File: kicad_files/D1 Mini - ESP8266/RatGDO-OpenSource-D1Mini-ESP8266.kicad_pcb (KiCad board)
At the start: 2 copper layers, 51.8 x 65.8 mm, 23 parts, among them J1 Screw_Terminal_01x03, J2 Conn_01x10, J3 Screw_Terminal_01x02, Q1 2N7002, Q2 AO3400A, Q3 AO3400A, Q4 AO3400A, U1 WeMos_D1_mini

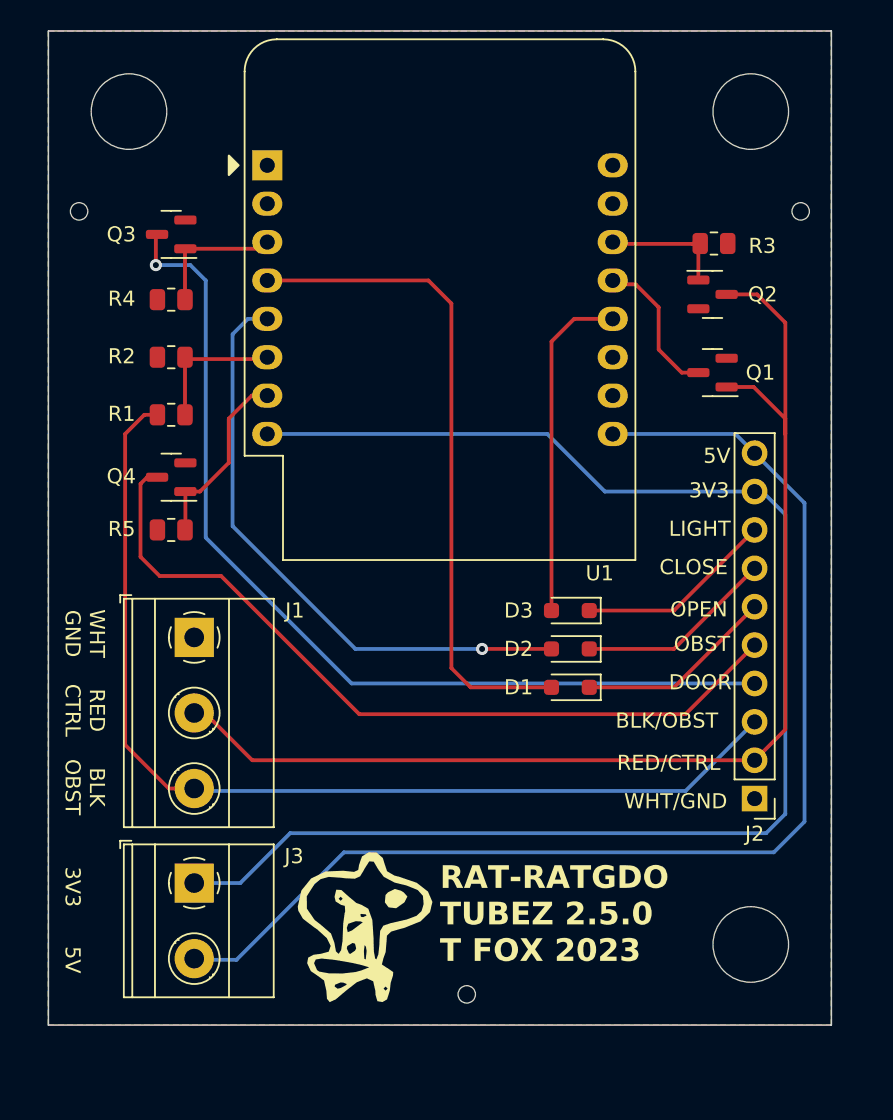
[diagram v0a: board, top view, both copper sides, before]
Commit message: Addition of 12V DC DC supply
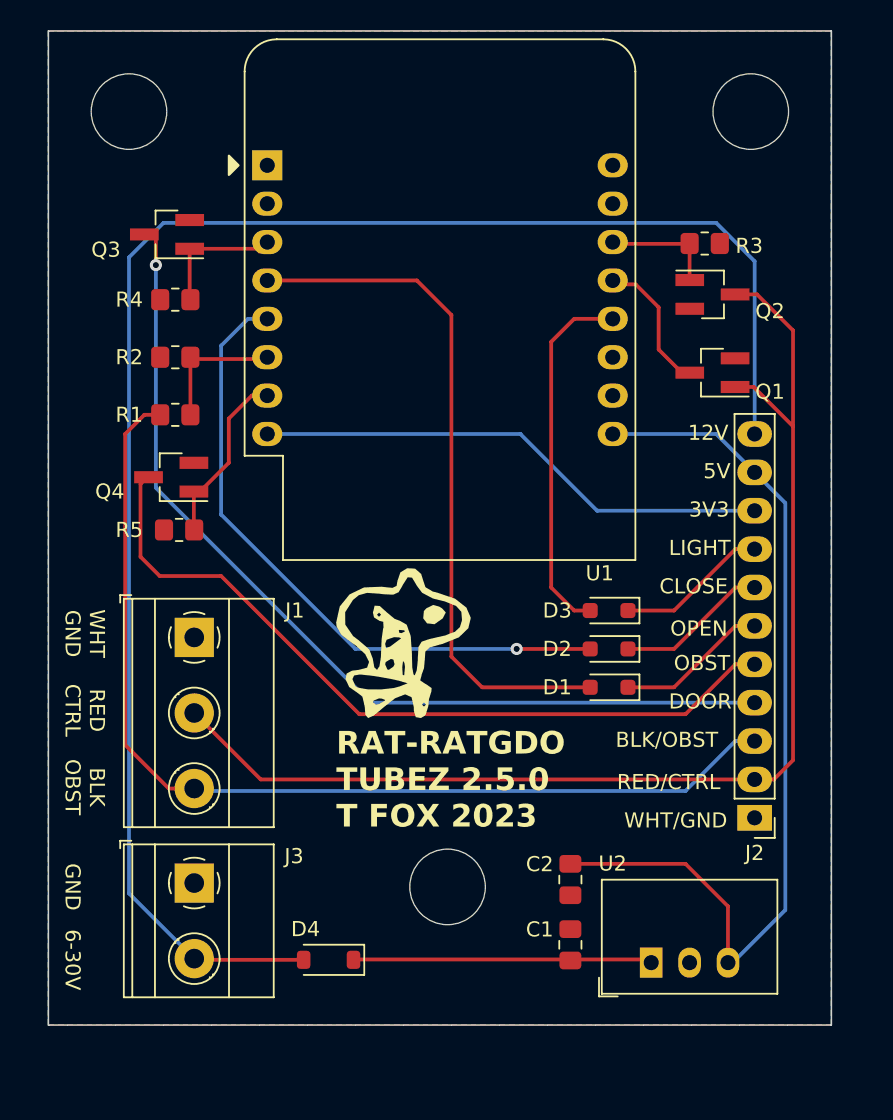
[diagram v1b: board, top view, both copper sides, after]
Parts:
- removed the REF** at (164.8, 69.1)
- removed the REF** at (117.1, 69.1)
- removed the REF** at (142.7, 120.9)
- added C1: 10uF/50V, Capacitor_SMD:C_0805_2012Metric_Pad1.18x1.45mm_HandSolder, F.Cu at (149.6, 117.6)
- added C2: 22uF/10V, Capacitor_SMD:C_0805_2012Metric_Pad1.18x1.45mm_HandSolder, F.Cu at (149.6, 113.3)
- added D4: B5819W, Diode_SMD:D_SOD-123, F.Cu at (133.6, 118.6)
- added U2: K7805-500R3, Converter_DCDC:Converter_DCDC_RECOM_R-78HB-0.5_THT, F.Cu at (160.0, 118.8)
- J2: value Conn_01x10 -> Conn_01x11; footprint Connector_PinHeader_2.54mm:PinHeader_1x10_P2.54mm_Vertical -> Connector_PinHeader_2.54mm:PinHeader_1x11_P2.54mm_Vertical
- Q1, Q2, Q3, Q4: footprint Package_TO_SOT_SMD:SOT-23 -> Package_TO_SOT_SMD:SOT-23_Handsoldering
- R1, R2, R3, R4, R5: footprint Resistor_SMD:R_0805_2012Metric -> Resistor_SMD:R_0805_2012Metric_Pad1.20x1.40mm_HandSolder
- moved REF** 20.4 mm to (141.5, 113.8)
- moved G*** 19.0 mm to (138.4, 97.5)
- moved D1 2.56 mm to (152.2, 100.6)
- moved D2 2.56 mm to (152.2, 98.0)
- moved D3 2.56 mm to (152.2, 95.5)
- moved J2 1.27 mm to (161.8, 109.2)
- moved R3 0.61 mm to (158.5, 71.2)
- moved R5 0.52 mm to (123.7, 90.2)
- moved Q3 0.28 mm to (122.9, 70.6)
- moved R1 0.27 mm to (123.5, 82.6)
- moved R2 0.27 mm to (123.5, 78.7)
- moved R4 0.27 mm to (123.5, 74.9)
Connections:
- J3 pad 1: +3V3 -> GND
- J3 pad 2: +5V -> +12V
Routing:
- net +12V: track 0.00 -> 109.9 mm
- net +3V3: track 96.1 -> 34.4 mm
- net Net-(D4-K): track 0.00 -> 19.7 mm
- net +5V: track 79.2 -> 60.7 mm
- net Net-(D2-A): track 39.9 -> 43.1 mm
- net DC_CLOSE: track 13.2 -> 10.1 mm
- net DC_OPEN: track 13.2 -> 10.1 mm
- net DC_LIGHT: track 13.2 -> 10.1 mm
- net RED/CTRL: track 79.0 -> 81.3 mm
- net Net-(D3-A): track 22.5 -> 24.2 mm
- net Net-(D1-A): track 44.1 -> 45.8 mm
- net /ESP_RX: track 9.84 -> 8.59 mm
- net STS_OBST: track 53.0 -> 51.8 mm
- net Net-(Q4-G): track 12.3 -> 11.3 mm
- net STS_DOOR: track 62.8 -> 62.0 mm
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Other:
- board text added: "12V"
- board text added: "6-30V"

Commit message: rename
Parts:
- removed C1: 10uF/50V, Capacitor_SMD:C_0805_2012Metric_Pad1.18x1.45mm_HandSolder
- removed C2: 22uF/10V, Capacitor_SMD:C_0805_2012Metric_Pad1.18x1.45mm_HandSolder
- removed D1, D2, D3: 1N4148WS, Diode_SMD:D_SOD-323_HandSoldering
- removed D4: B5819W, Diode_SMD:D_SOD-123
- removed G***: LOGO, LOGO
- removed Q3, Q4: AO3400A, Package_TO_SOT_SMD:SOT-23_Handsoldering
- removed R4, R5: 10k, Resistor_SMD:R_0805_2012Metric_Pad1.20x1.40mm_HandSolder
- removed U2: K7805-500R3, Converter_DCDC:Converter_DCDC_RECOM_R-78HB-0.5_THT
- added REF**: MountingHole_5mm, MountingHole:MountingHole_5mm, F.Cu at (120.7, 118.1)
- J2: value Conn_01x11 -> Screw_Terminal_01x03; footprint Connector_PinHeader_2.54mm:PinHeader_1x11_P2.54mm_Vertical -> Connector_Phoenix_MC:PhoenixContact_MCV_1,5_3-G-3.5_1x03_P3.50mm_Vertical
- J3: value Screw_Terminal_01x02 -> Screw_Terminal_01x03; footprint TerminalBlock_Phoenix:TerminalBlock_Phoenix_MKDS-1,5-2_1x02_P5.00mm_Horizontal -> Connector_PinSocket_2.54mm:PinSocket_1x03_P2.54mm_Vertical
- Q1, Q2: footprint Package_TO_SOT_SMD:SOT-23_Handsoldering -> Package_TO_SOT_SMD:SOT-23
- R1, R2, R3: footprint Resistor_SMD:R_0805_2012Metric_Pad1.20x1.40mm_HandSolder -> Resistor_SMD:R_0805_2012Metric
- moved J3 22.7 mm to (147.3, 111.8), turned to 90 degrees
- moved J1 21.7 mm to (129.7, 118.4), turned to 0 degrees
- moved REF** 21.5 mm to (162.6, 118.1)
- moved J2 18.2 mm to (146.7, 119.4), turned to 0 degrees
- moved REF** 1.44 mm to (162.6, 63.5)
- moved REF** 1.05 mm to (120.7, 63.5)
- moved R1 0.27 mm to (123.2, 82.5)
- moved R2 0.27 mm to (123.2, 78.7)
- moved Q1 0.15 mm to (159.2, 79.8)
- moved R3 0.14 mm to (158.6, 71.2), turned to 180 degrees
- moved U1 0.12 mm to (129.5, 66.2)
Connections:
- net /ESP_RX renamed Net-(Q1-D)
- J1 pad 1: GND -> Net-(J1-Blk/Obst)
- J1 pad 2: RED/CTRL -> Net-(J1-Red/Cntrl)
- J1 pad 3: BLK/OBST -> GND
- J2 pad 1: GND -> Net-(J1-Blk/Obst)
- J2 pad 2: RED/CTRL -> Net-(J1-Red/Cntrl)
- J2 pad 3: BLK/OBST -> GND
- J3 pad 1: GND -> Net-(J1-Blk/Obst)
- J3 pad 2: +12V -> Net-(J1-Red/Cntrl)
- Q1 pad 1: RED/CTRL -> Net-(J1-Red/Cntrl)
- Q2 pad 1: /ESP_TX -> Net-(Q2-G)
- Q2 pad 3: RED/CTRL -> Net-(J1-Red/Cntrl)
- R1 pad 1: BLK/OBST -> Net-(J1-Blk/Obst)
- R3 pad 1: /ESP_TX -> GND
- R3 pad 2: GND -> Net-(Q2-G)
- U1 pad 12: Net-(D3-A) -> unconnected-(U1-D3-Pad12)
- U1 pad 14: /ESP_TX -> Net-(Q2-G)
- U1 pad 3: Net-(Q3-G) -> unconnected-(U1-D0-Pad3)
- U1 pad 4: Net-(D1-A) -> unconnected-(U1-SCK/D5-Pad4)
- U1 pad 5: Net-(D2-A) -> unconnected-(U1-MISO/D6-Pad5)
- U1 pad 7: Net-(Q4-G) -> unconnected-(U1-CS/D8-Pad7)
- U1 pad 8: +3V3 -> +3.3V
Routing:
- net +12V: track 109.9 -> 0.00 mm
- net RED/CTRL: track 81.3 -> 0.00 mm
- net Net-(J1-Blk/Obst): track 0.00 -> 77.8 mm
- net Net-(J1-Red/Cntrl): track 0.00 -> 69.3 mm
- net BLK/OBST: track 65.7 -> 0.00 mm
- net STS_DOOR: track 62.0 -> 0.00 mm, vias 1 -> 0
- net +5V: track 60.7 -> 0.00 mm
- net STS_OBST: track 51.8 -> 0.00 mm
- net Net-(D1-A): track 45.8 -> 0.00 mm
- net Net-(D2-A): track 43.1 -> 0.00 mm, vias 1 -> 0
- net +3V3: track 34.4 -> 0.00 mm
- net Net-(D3-A): track 24.2 -> 0.00 mm
- net Net-(D4-K): track 19.7 -> 0.00 mm
- net Net-(Q4-G): track 11.3 -> 0.00 mm
- net DC_OPEN: track 10.1 -> 0.00 mm
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- removed copper zone on F.Cu, net GND
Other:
- board size 51.8 x 65.8 mm -> 55 x 70 mm
- board text added: "5v"
- board text added: "EN"
- board text added: "GPIO0"
- board text added: "GPIO1"
- board text added: "GPIO12"
- board text added: "GPIO13"
- board text added: "GPIO14"
- board text added: "GPIO15"
- board text added: "GPIO16"
- board text added: "GPIO2"
- board text added: "GPIO3"
- board text added: "GPIO4"
- board text added: "GPIO5"
- board text added: "Only 1 Terminal Block Needs Populated. The Choice Is Yours."
- board text added: "VCC-3v3"
- board text removed: "12V"
- board text removed: "3V3"
- board text removed: "5V"
- board text removed: "6-30V"
- board text removed: "A0"
- board text removed: "BLK/OBST"
- board text removed: "CLOSE"
- board text removed: "D0"
- board text removed: "D1/SCL"
- board text removed: "D2/SDA"
- board text removed: "D3"
- board text removed: "D4"
- board text removed: "D5/SCK"
- board text removed: "D6/MISO"
- board text removed: "D7/MOSI"
- board text removed: "D8"
- board text removed: "DOOR"
- board text removed: "JLCJLCJLCJLC"
- board text removed: "LIGHT"
- board text removed: "OBST"
- board text removed: "OPEN"
- board text removed: "RAT-RATGDO TUBEZ 2.5.0 T FOX 2023"
- board text removed: "RED/CTRL"
- board text removed: "RX"
- board text removed: "TX"
- board text removed: "WHT/GND"

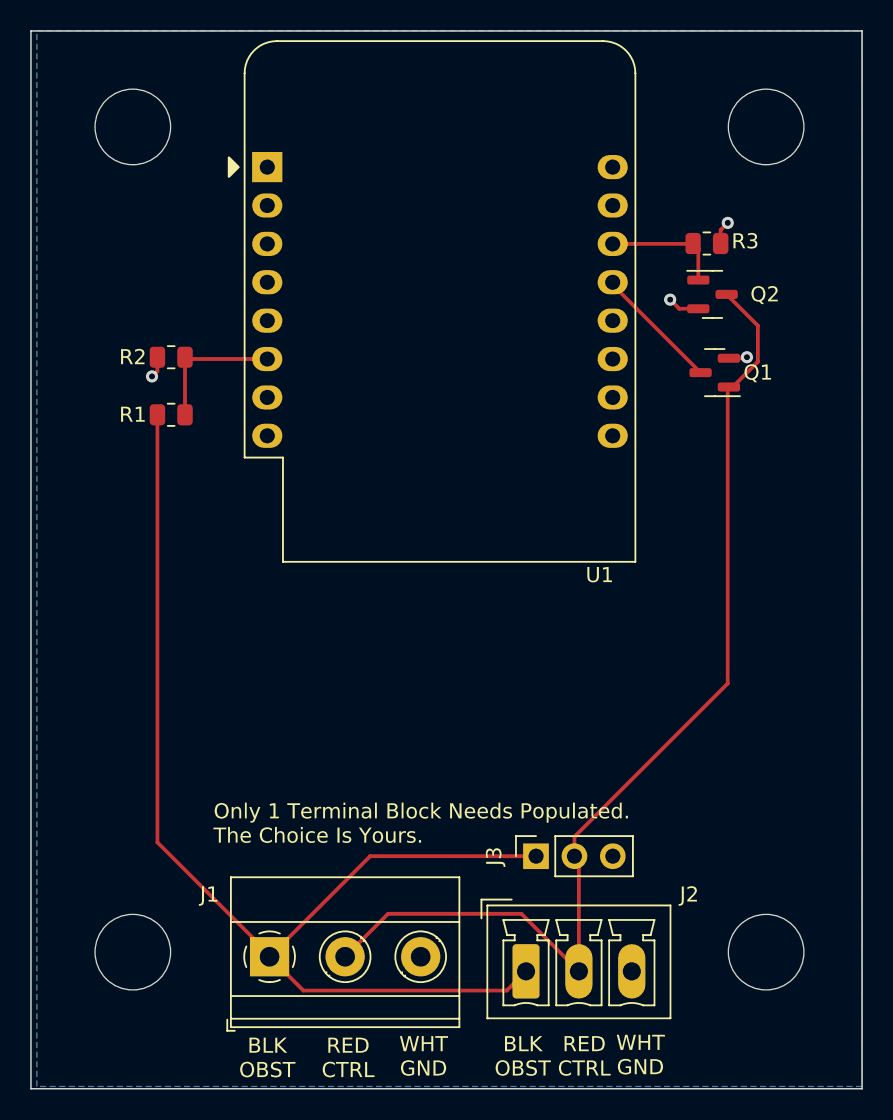
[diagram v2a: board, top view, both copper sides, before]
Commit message: add extra output/input like original ratgdo v2.5
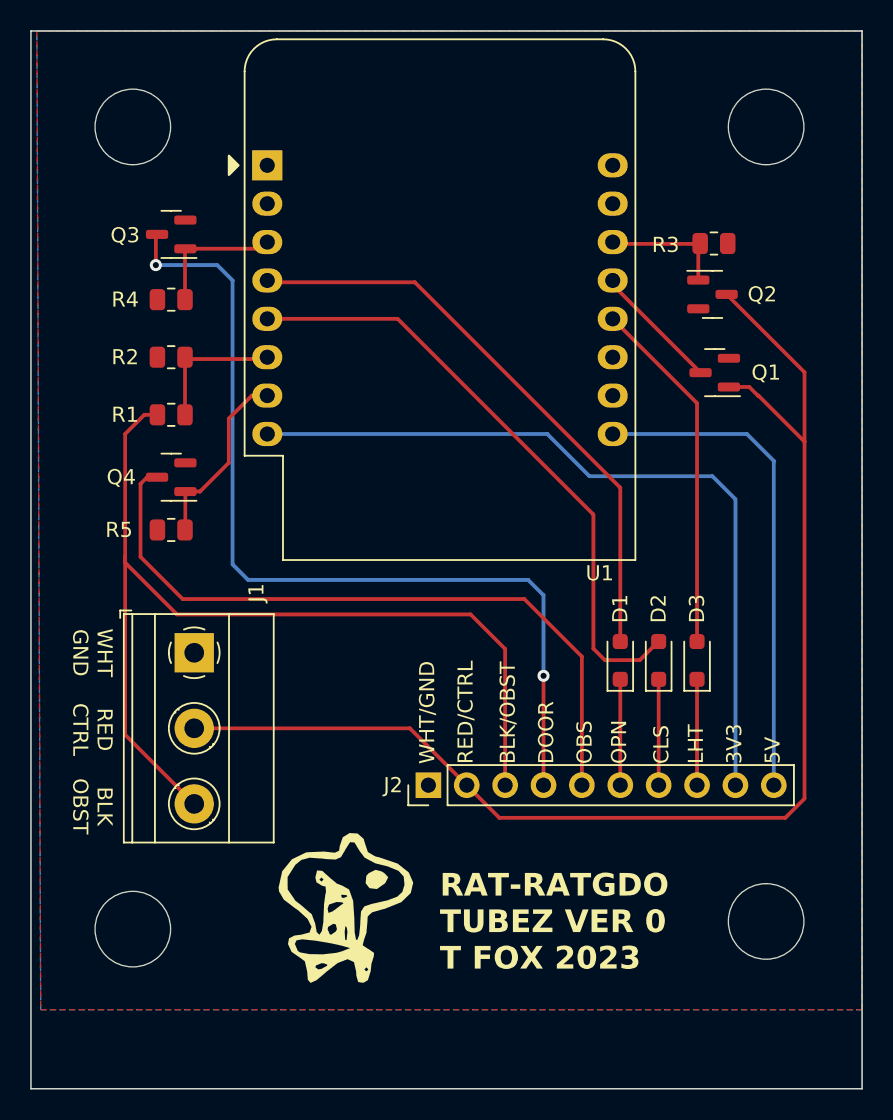
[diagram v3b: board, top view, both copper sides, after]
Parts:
- removed J3: Screw_Terminal_01x03, Connector_PinSocket_2.54mm:PinSocket_1x03_P2.54mm_Vertical
- added D1: 1N4148WS, Diode_SMD:D_SOD-323_HandSoldering, F.Cu at (152.9, 98.8)
- added D2: 1N4148WS, Diode_SMD:D_SOD-323_HandSoldering, F.Cu at (155.4, 98.8)
- added D3: 1N4148WS, Diode_SMD:D_SOD-323_HandSoldering, F.Cu at (158.0, 98.8)
- added G***: LOGO, LOGO, F.Cu at (134.6, 115.1)
- added Q3: AO3400A, Package_TO_SOT_SMD:SOT-23, F.Cu at (123.2, 70.6)
- added Q4: AO3400A, Package_TO_SOT_SMD:SOT-23, F.Cu at (123.2, 86.7)
- added R4: 10k, Resistor_SMD:R_0805_2012Metric, F.Cu at (123.2, 74.9)
- added R5: 10k, Resistor_SMD:R_0805_2012Metric, F.Cu at (123.2, 90.2)
- J2: value Screw_Terminal_01x03 -> Conn_01x10; footprint Connector_Phoenix_MC:PhoenixContact_MCV_1,5_3-G-3.5_1x03_P3.50mm_Vertical -> Connector_PinHeader_2.54mm:PinHeader_1x10_P2.54mm_Vertical
- moved J1 20.7 mm to (124.7, 98.3), turned to -90 degrees
- moved J2 13.9 mm to (140.2, 107.1), turned to 90 degrees
- moved REF** 2.03 mm to (162.6, 116.1)
- moved REF** 1.52 mm to (120.7, 116.6)
- moved R3 0.47 mm to (159.1, 71.2), turned to 0 degrees
- moved U1 0.12 mm to (129.5, 66.0)
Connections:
- net Net-(J1-Red/Cntrl) renamed RED/CTRL
- J1 pad 1: Net-(J1-Blk/Obst) -> GND
- J1 pad 3: GND -> BLK/OBST
- J2 pad 1: Net-(J1-Blk/Obst) -> GND
- J2 pad 3: GND -> BLK/OBST
- R1 pad 1: Net-(J1-Blk/Obst) -> BLK/OBST
- R3 pad 1: GND -> Net-(Q2-G)
- R3 pad 2: Net-(Q2-G) -> GND
- U1 pad 12: unconnected-(U1-D3-Pad12) -> Net-(D3-A)
- U1 pad 3: unconnected-(U1-D0-Pad3) -> Net-(Q3-G)
- U1 pad 4: unconnected-(U1-SCK/D5-Pad4) -> Net-(D1-A)
- U1 pad 5: unconnected-(U1-MISO/D6-Pad5) -> Net-(D2-A)
- U1 pad 7: unconnected-(U1-CS/D8-Pad7) -> Net-(Q4-G)
- U1 pad 8: +3.3V -> +3V3
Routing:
- net Net-(J1-Blk/Obst): track 77.8 -> 0.00 mm
- net BLK/OBST: track 0.00 -> 65.9 mm
- net STS_DOOR: track 0.00 -> 60.0 mm, vias 0 -> 2
- net +3V3: track 0.00 -> 51.7 mm
- net STS_OBST: track 0.00 -> 46.6 mm
- net Net-(D2-A): track 0.00 -> 41.0 mm
- net Net-(D1-A): track 0.00 -> 39.2 mm
- net +5V: track 0.00 -> 32.9 mm
- net Net-(D3-A): track 0.00 -> 23.7 mm
- net RED/CTRL: track 69.3 -> 85.4 mm
- net Net-(Q4-G): track 0.00 -> 12.3 mm
- net Net-(Q3-G): track 0.00 -> 8.86 mm
- net DC_OPEN: track 0.00 -> 7.01 mm
- net DC_LIGHT: track 0.00 -> 7.01 mm
- net DC_CLOSE: track 0.00 -> 7.01 mm
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- added copper zone on F.Cu, net GND
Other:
- board text added: "3V3"
- board text added: "5V"
- board text added: "BLK/OBST"
- board text added: "CLS"
- board text added: "DOOR"
- board text added: "LHT"
- board text added: "OBS"
- board text added: "OPN"
- board text added: "RAT-RATGDO TUBEZ VER 0 T FOX 2023"
- board text added: "RED/CTRL"
- board text added: "WHT/GND"
- board text removed: "Only 1 Terminal Block Needs Populated. The Choice Is Yours."

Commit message: laid out pcba with new outline and keepout
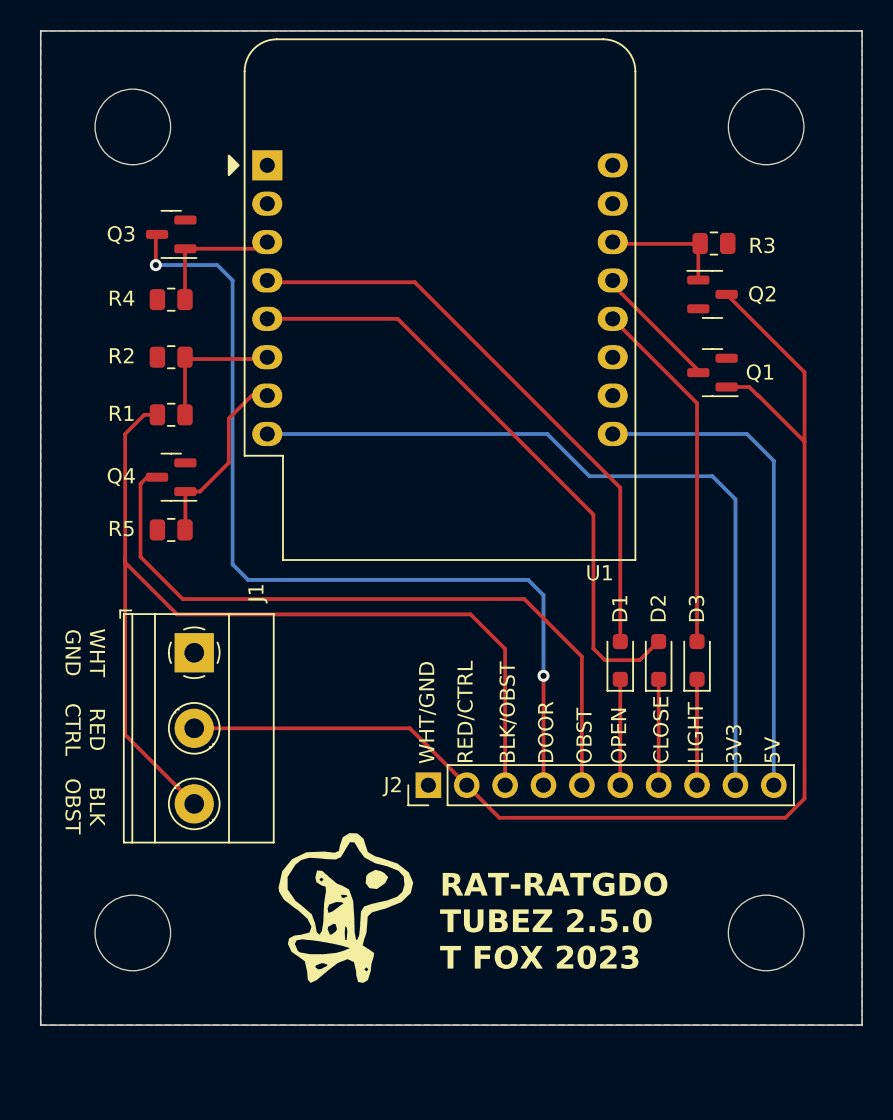
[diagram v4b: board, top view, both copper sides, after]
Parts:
- moved REF** 0.76 mm to (162.6, 116.8)
- moved REF** 0.25 mm to (120.7, 116.8)
- moved Q1 0.15 mm to (159.0, 79.8)
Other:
- board size 55 x 70 mm -> 54.4 x 65.8 mm
- board text added: "CLOSE"
- board text added: "LIGHT"
- board text added: "OBST"
- board text added: "OPEN"
- board text added: "RAT-RATGDO TUBEZ 2.5.0 T FOX 2023"
- board text removed: "CLS"
- board text removed: "LHT"
- board text removed: "OBS"
- board text removed: "OPN"
- board text removed: "RAT-RATGDO TUBEZ VER 0 T FOX 2023"
